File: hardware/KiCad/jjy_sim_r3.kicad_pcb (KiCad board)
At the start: 2 copper layers, 65 x 100 mm, 92 parts, among them P1 USB_C_Plug_USB2.0, Q1 HN1C01FU-GR, SW1 RESET, SW2 CONFIG, SW3 BAND, U1 AM1025EA, U2 ESP32-C3-WROOM-02/ESP8684-WRO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, U3 RT9193-33GB, U4 UG-2864HL, U5 CH340K

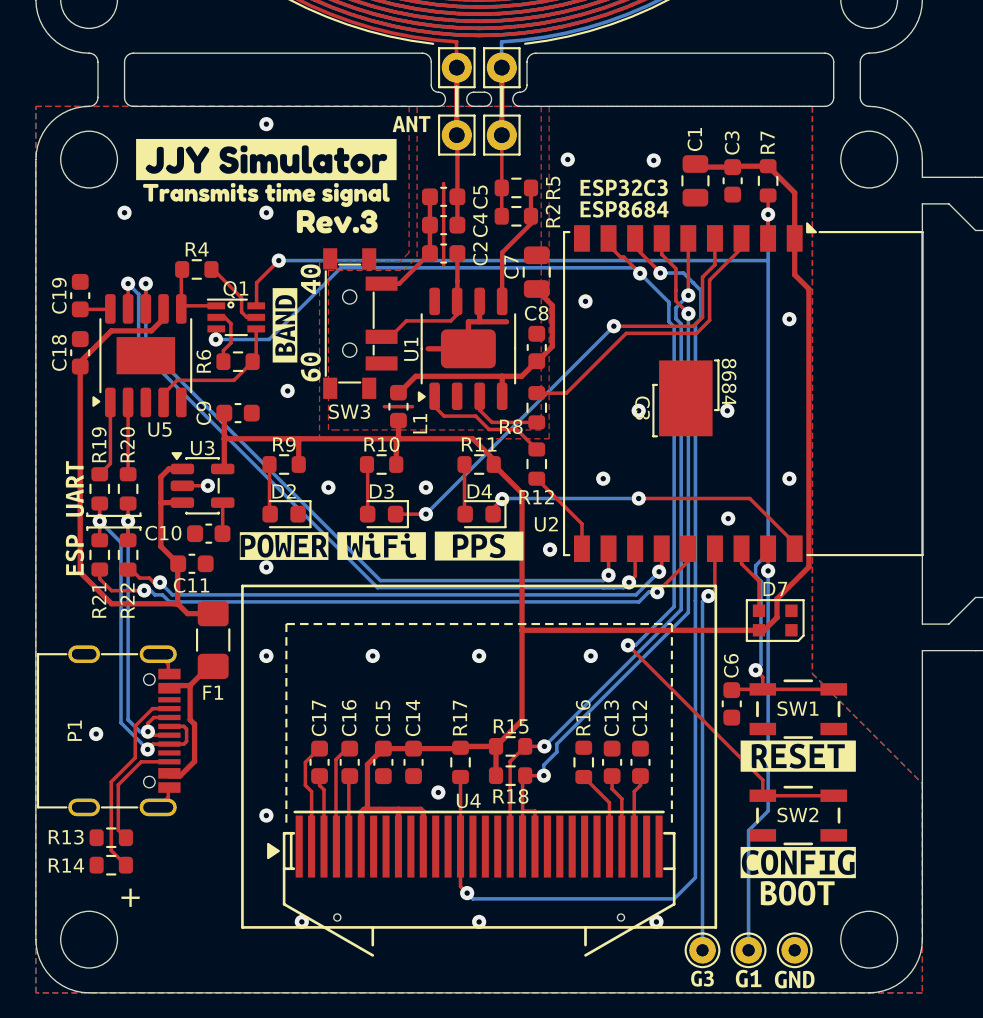
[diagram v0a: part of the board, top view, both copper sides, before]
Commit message: Update project for KiCad 10.0 and add local libraries
- Updated KiCad project files for KiCad 10.0
- Moved the BAND-SW position
- Added project-local KiCad libraries
- Included custom libraries that were previously not committed
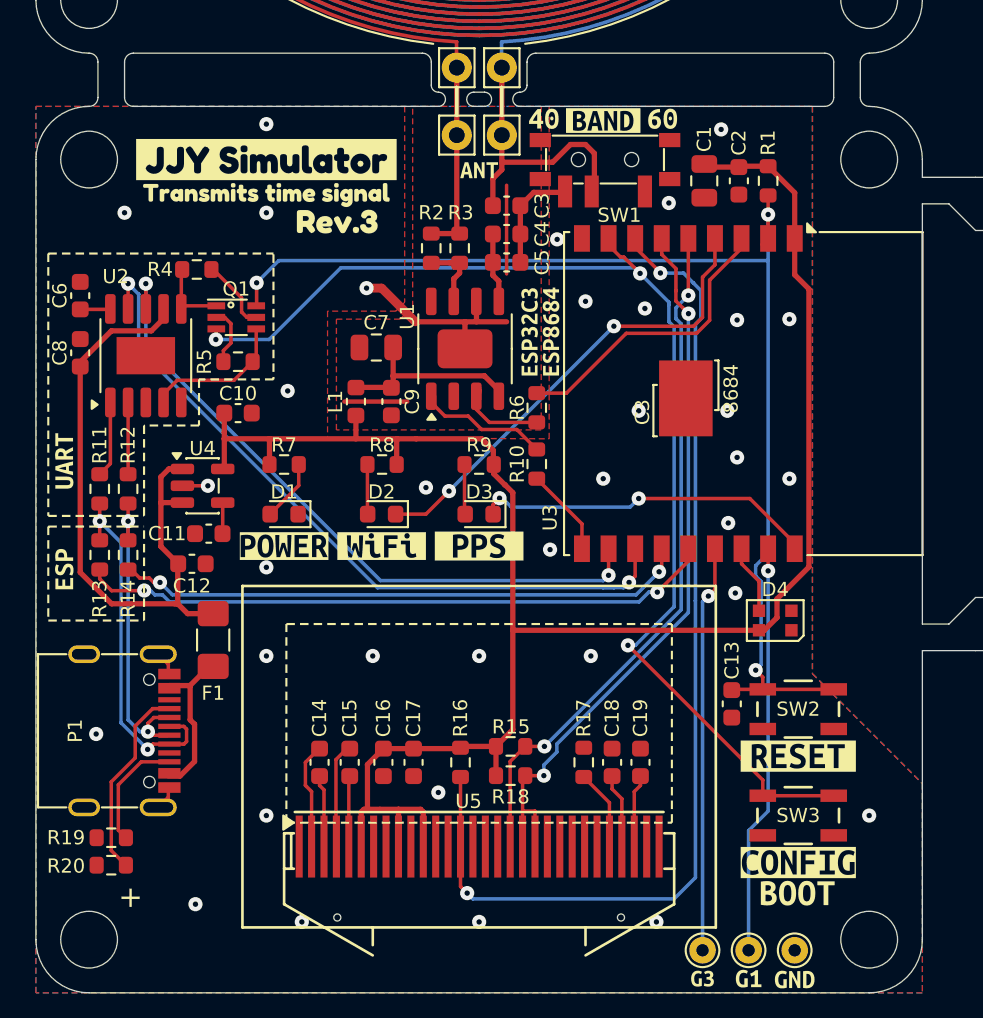
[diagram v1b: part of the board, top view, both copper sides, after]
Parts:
- added kibuzzard-6A179A92: G***, kibuzzard-6A179A92, B.Cu at (110.7, 148.7)
- G***: footprint MY_LOGO:ORCA_LOGO_15mm -> JJY-SIM-R3:Shachi-lab_LOGO_15mm
- G***1: renamed from G***; footprint MY_LOGO:ORCA_LOGO_15mm -> JJY-SIM-R3:Shachi-lab_LOGO_15mm
- JP1, JP2: footprint MY_LIB:Jumper-2_TH_3.81mm -> JJY-SIM-R3:Jumper-2_TH_3.81mm
- P1: footprint MY_LIB:5077CR-16SMC2-BK-TR -> JJY-SIM-R3:5077CR-16SMC2-BK-TR_Ext
- Q1: footprint MY_LIB:2-2J1A -> JJY-SIM-R3:2-2J1A
- REF**1: renamed from REF**; footprint MY_LIB:UG-2864-DISP -> JJY-SIM-R3:UG-2864-DISP
- SW1: renamed from SW3; footprint MY_LIB:MSK-12C02 -> JJY-SIM-R3:MSK-12C02
- SW2: renamed from SW1; footprint MY_LIB:SKRPACE010 -> JJY-SIM-R3:SKRPACE010
- SW3: renamed from SW2; footprint MY_LIB:SKRPACE010 -> JJY-SIM-R3:SKRPACE010
- U1: footprint MY_LIB:eSOP-8_3.9x5.05mm_EP_3.1x2.2mm_P1.27mm -> JJY-SIM-R3:eSOP-8_3.9x5.05mm_EP_3.1x2.2mm_P1.27mm
- U2: renamed from U5; footprint Package_SO:SSOP-10-1EP_3.9x4.9mm_P1mm_EP2.1x3.3mm -> JJY-SIM-R3:SSOP-10-1EP_3.9x4.9mm_P1mm_EP2.1x3.3mm
- U3: renamed from U2; value ESP32-C3-WROOM-02/ESP8684-WROOM-2C -> ESP32-C3-WROOM-02; footprint MY_LIB:ESP32-C3-WROOM-02,ESP8684-WROOM-2C -> JJY-SIM-R3:ESP32-C3-WROOM-02,ESP8684-WROOM-2C
- U5: renamed from U4; footprint MY_LIB:UG-2864-FPC (Reverse) -> JJY-SIM-R3:UG-2864-FPC (Reverse)
- moved kibuzzard-3 24.3 mm to (135.3, 100.7), turned to 0 degrees
- moved kibuzzard-4 21.3 mm to (132.0, 100.8), turned to 0 degrees
- moved SW1 17.1 mm to (132.1, 103.0), turned to 0 degrees
- moved kibuzzard-2 16.0 mm to (128.7, 100.7), turned to 0 degrees
- moved C7 10.00 mm to (119.2, 113.6), turned to 180 degrees
- moved kibuzzard-9 8.88 mm to (128.4, 112.7), turned to 90 degrees
- moved C9 8.75 mm to (120.0, 116.7), turned to -90 degrees
- moved R2 5.88 mm to (122.3, 108.0), turned to -90 degrees
- moved C5 5.13 mm to (126.5, 108.8)
- moved kibuzzard-6 4.61 mm to (125.0, 103.6)
- moved C3 4.46 mm to (126.5, 105.6)
- moved R3 3.67 mm to (123.9, 108.0), turned to -90 degrees
- moved C4 3.59 mm to (126.5, 107.2)
- moved L1 2.42 mm to (118.0, 116.7)
- moved kibuzzard-10 1.69 mm to (101.6, 120.0)
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- gave numbers to parts that had none: 8
- renumbered C9 to C10, C10 to C11, C11 to C12, C6 to C13, C17 to C14, C16 to C15, C15 to C16, C14 to C17, C13 to C18, C12 to C19, C3 to C2, C2 to C3, C19 to C6, C18 to C8, C8 to C9, D2 to D1, D3 to D2, D4 to D3, D7 to D4, R7 to R1, R12 to R10, R19 to R11, R20 to R12, R21 to R13, R22 to R14, R17 to R16, R16 to R17, R13 to R19, R5 to R2, R14 to R20, R2 to R3, R6 to R5, R8 to R6, R9 to R7, R10 to R8, R11 to R9, U3 to U4, kibuzzard-28 to kibuzzard-1, kibuzzard-698209E3 to kibuzzard-10, kibuzzard-14 to kibuzzard-11, kibuzzard-15 to kibuzzard-12, kibuzzard-68E061D7 to kibuzzard-13, kibuzzard-69965DBC to kibuzzard-14, kibuzzard-17 to kibuzzard-15, kibuzzard-19 to kibuzzard-16, kibuzzard-20 to kibuzzard-17, kibuzzard-21 to kibuzzard-18, kibuzzard-22 to kibuzzard-19, kibuzzard-6982098F to kibuzzard-2, kibuzzard-23 to kibuzzard-20, kibuzzard-69820977 to kibuzzard-3, kibuzzard-69820ADF to kibuzzard-4, kibuzzard-68D3A9C1 to kibuzzard-5, kibuzzard-1 to kibuzzard-6, kibuzzard-68D3A910 to kibuzzard-7, kibuzzard-69816480 to kibuzzard-8, kibuzzard-69867CAB to kibuzzard-9
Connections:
- C3 pad 1: Net-(SW3-B) -> Net-(SW3-A)
- C3 pad 2: Net-(SW3-C) -> /RF_B
- C4 pad 1: Net-(SW3-C) -> Net-(U1-OUT_B)
- C4 pad 2: /RF_A -> Net-(SW3-A)
- C5 pad 1: Net-(SW3-C) -> Net-(U1-OUT_B)
- C5 pad 2: /RF_A -> Net-(SW3-A)
- R2 pad 1: /RF_B -> /RF_A
- R2 pad 2: Net-(U1-OUT_B) -> Net-(U1-OUT_A)
- R3 pad 1: /RF_B -> /RF_A
- R3 pad 2: Net-(U1-OUT_B) -> Net-(U1-OUT_A)
- SW1 pad 1: unconnected-(SW3-A-Pad1) -> Net-(SW3-A)
- SW1 pad 2: Net-(SW3-B) -> /RF_B
- SW1 pad 3: Net-(SW3-C) -> unconnected-(SW3-C-Pad3)
- U1 pad 7: Net-(SW3-B) -> Net-(U1-OUT_A)
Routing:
- net Net-(SW3-B): track 8.23 -> 0.00 mm
- net /RF_B: track 4.61 -> 12.2 mm
- net GND: track 17.8 -> 24.4 mm, vias 28 -> 35
- net Net-(SW3-C): track 6.63 -> 0.00 mm
- net Net-(SW3-A): track 0.00 -> 6.32 mm
- net Net-(U1-OUT_A): track 0.00 -> 3.94 mm
- net /RF_PWR: track 14.6 -> 11.3 mm
- net Net-(U1-OUT_B): track 7.07 -> 3.94 mm
- net /RF_A: track 5.04 -> 7.15 mm
- net Net-(D2-A): track 2.82 -> 3.52 mm
- net +3V3: track 108.5 -> 109.2 mm
- net Net-(U1-IN_A): track 7.35 -> 7.99 mm
- net GPIO0: track 18.9 -> 19.5 mm
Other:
- board text removed: "OLED base"
